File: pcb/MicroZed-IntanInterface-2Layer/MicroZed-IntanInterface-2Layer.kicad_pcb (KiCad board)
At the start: 2 copper layers, 100.3 x 135.4 mm, 107 parts, among them J1 Screw_Terminal_01x02, J2 Conn_02x05_Odd_Even, J4 USB_C_Receptacle_USB2.0_16P, J7 GND header for probes, Q1 BSS138, Q2 BSS138, Q3 BSS138, Q4 BSS138, SW1 SW_MEC_5E, SW2 SW_MEC_5E, U1 AP331A, U2 TLV62568DDC, U3 FT230XS, U9 TLV62568DDC

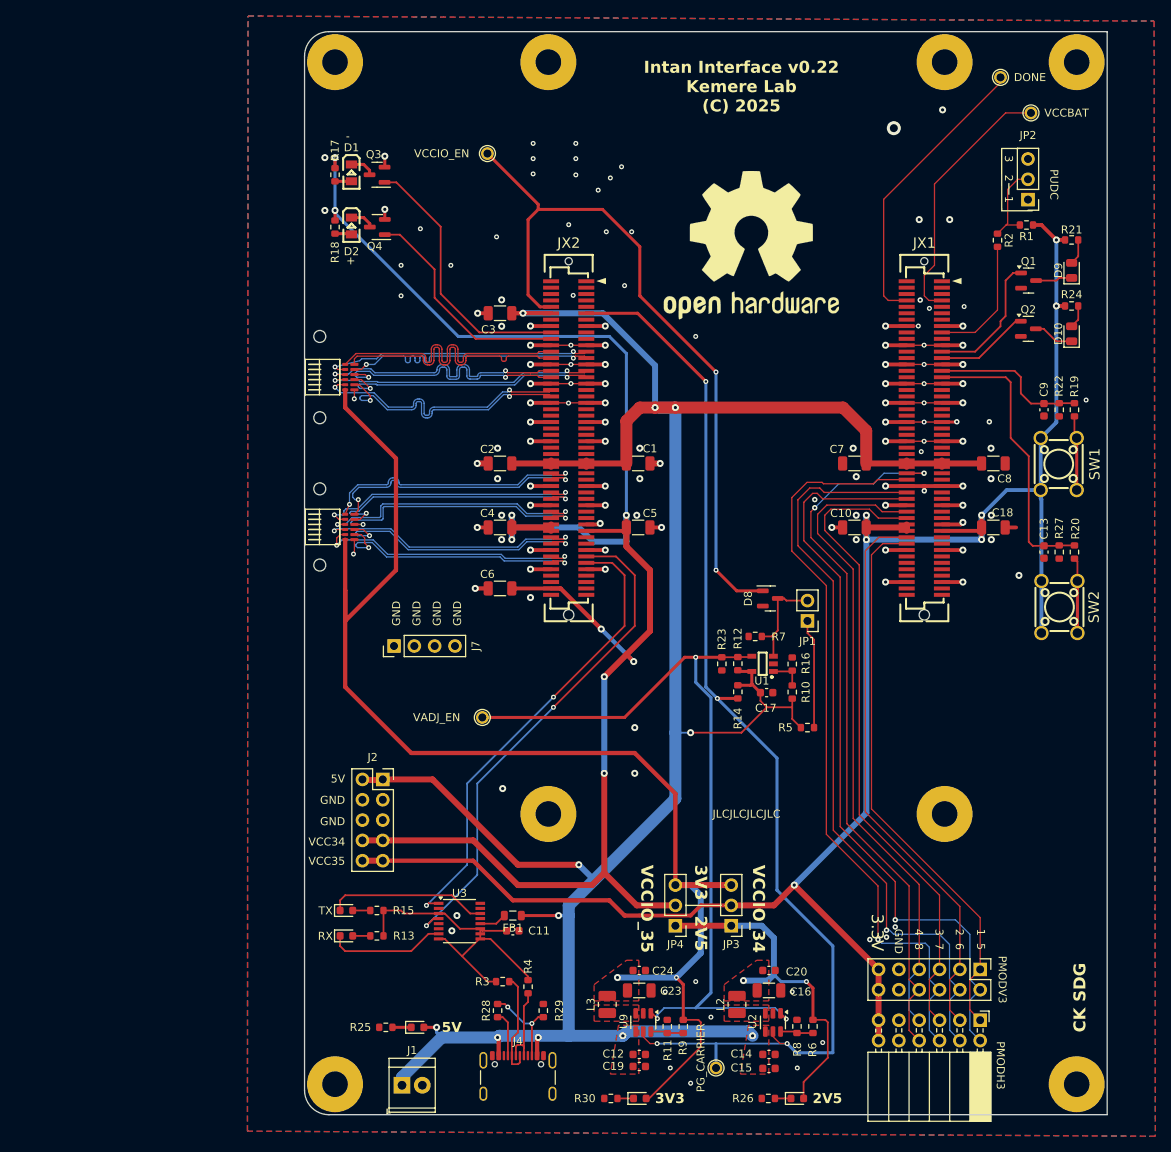
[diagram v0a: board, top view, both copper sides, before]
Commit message: Updated PCB after v0.22 bug fixes
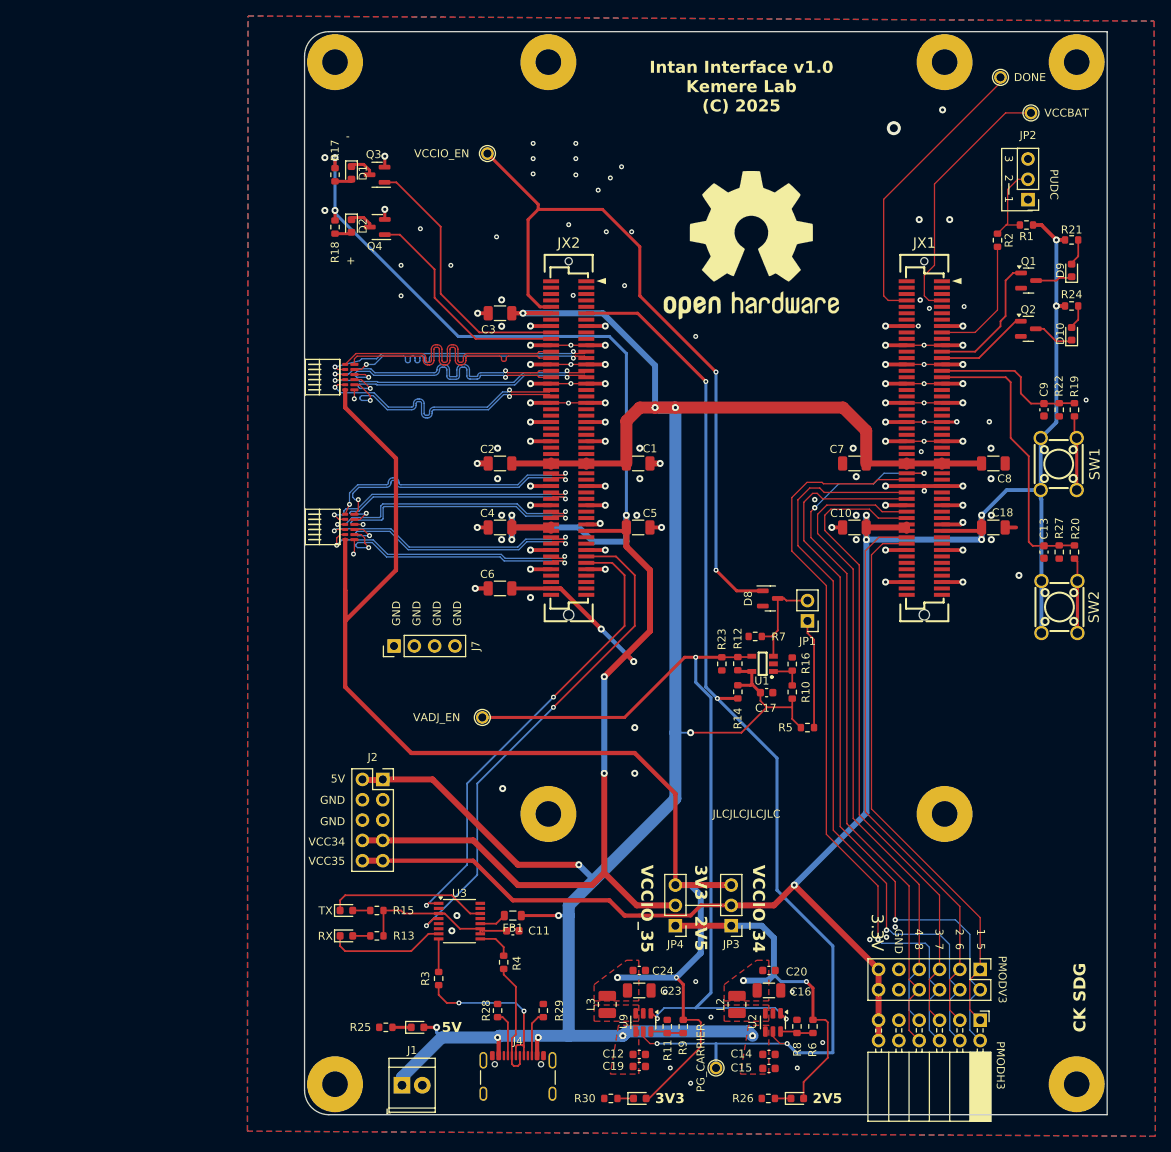
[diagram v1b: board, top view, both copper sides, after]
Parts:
- removed REF** (x4): MountingHole_2.1mm, MountingHole:MountingHole_2.1mm
- D1: value LED yellow -> LED0; footprint Viktor:LED0805 -> LED_SMD:LED_0603_1608Metric
- D10: value LED 4 -> LED3; footprint LED_SMD:LED_0805_2012Metric -> LED_SMD:LED_0603_1608Metric
- D2: value LED yellow -> LED1; footprint Viktor:LED0805 -> LED_SMD:LED_0603_1608Metric
- D9: value LED 3 -> LED2; footprint LED_SMD:LED_0805_2012Metric -> LED_SMD:LED_0603_1608Metric
- moved R3 8.01 mm to (52.3, 166.6), turned to 90 degrees
- moved R4 4.31 mm to (60.5, 164.6)
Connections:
- JX1 pad 23: /JX1_connections/LED3 -> /JX1_connections/LED2
- JX1 pad 25: /JX1_connections/LED4 -> /JX1_connections/LED3
- JX2 pad 18: /JX2_connections/LED1 -> /JX2_connections/LED0
- JX2 pad 20: /JX2_connections/LED2 -> /JX2_connections/LED1
- Q1 pad 1: /JX1_connections/LED3 -> /JX1_connections/LED2
- Q2 pad 1: /JX1_connections/LED4 -> /JX1_connections/LED3
- Q3 pad 1: /JX2_connections/LED1 -> /JX2_connections/LED0
- Q4 pad 1: /JX2_connections/LED2 -> /JX2_connections/LED1
- R28 pad 2: Net-(J4-CC2) -> GND
- R3 pad 1: USB_D- -> USB_D+
- R3 pad 2: Net-(U3-3V3OUT) -> Net-(U3-USBDP)
- R4 pad 1: USB_D+ -> USB_D-
- R4 pad 2: Net-(U3-3V3OUT) -> Net-(U3-USBDM)
- U3 pad 8: Net-(U3-3V3OUT) -> Net-(U3-USBDP)
- U3 pad 9: Net-(U3-3V3OUT) -> Net-(U3-USBDM)
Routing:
- net /JX2_connections/LED0: track 0.00 -> 33.5 mm
- net /JX2_connections/LED2: track 28.3 -> 0.00 mm
- net Net-(U3-3V3OUT): track 41.8 -> 20.3 mm
- net /JX1_connections/LED2: track 0.00 -> 16.9 mm
- net /JX1_connections/LED4: track 11.8 -> 0.00 mm
- net USB_D+: track 10.5 -> 20.6 mm, vias 0 -> 2
- net Net-(J4-CC2): track 11.1 -> 5.78 mm, vias 2 -> 0
- net /JX2_connections/LED1: track 33.5 -> 28.3 mm
- net /JX1_connections/LED3: track 16.9 -> 11.8 mm
- net Net-(U3-USBDM): track 0.00 -> 4.43 mm
- net Net-(U3-USBDP): track 0.00 -> 4.13 mm
- net USB_D-: track 13.3 -> 15.0 mm
- net VCCIO_35: track 221.2 -> 220.5 mm
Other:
- board text added: "Intan Interface v1.0 Kemere Lab (C) 2025"
- board text removed: "Intan Interface v0.22 Kemere Lab (C) 2025"

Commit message: Updates for version 1.0 to ship to UMich
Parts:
- removed JP1: Jumper_2_Open, Connector_PinHeader_2.54mm:PinHeader_1x02_P2.54mm_Vertical
- removed JP3, JP4: Jumper_3_Bridged12, Connector_PinHeader_2.54mm:PinHeader_1x03_P2.54mm_Vertical
- removed OpenHW logo: OSHW-Logo2_24.3x20mm_SilkScreen, Symbol:OSHW-Logo2_24.3x20mm_SilkScreen
- added JP5: SolderJumper_2_Open, Jumper:SolderJumper-2_P1.3mm_Open_RoundedPad1.0x1.5mm, B.Cu at (101.6, 86.6)
- added REF**: RICE_OWL_LOGO, ELEC327-Kicad:RICE_OWL_LOGO, F.Cu at (46.5, 78.0)
- added REF**: RICE_OWL_LOGO, ELEC327-Kicad:RICE_OWL_LOGO, F.Cu at (88.1, 114.0)
- added SW3: SW_SPDT, Button_Switch_SMD:SW_SPDT_PCM12, F.Cu at (101.6, 146.1)
- added SW4: SW_SPDT, Button_Switch_SMD:SW_SPDT_PCM12, F.Cu at (82.5, 146.1)
- C1, C16, C23: value 22uF 10V -> 22uF 25V
- C10, C18, C2, C3, C4, C5, C6, C7, C8: value 22uF -> 22uF 25V
- C11, C13, C15, C17, C19, C20, C24, C9: footprint Capacitor_SMD:C_0603_1608Metric -> Capacitor_SMD:C_0402_1005Metric
- H1, H2, H3, H4, H5, H6, H7, H8: footprint Viktor:MountingHole_3.2mm_Pad_7mm -> MountingHole:MountingHole_3.2mm_M3_Pad
- JP2: moved to B.Cu
- L2, L3: footprint Inductor_SMD:L_1008_2520Metric -> Inductor_SMD:L_1210_3225Metric
- R1, R5: value 1K -> 1k 1%; footprint Resistor_SMD:R_0603_1608Metric -> Resistor_SMD:R_0402_1005Metric
- R10: value 5K6 1% -> 5.6k 1%; footprint Resistor_SMD:R_0603_1608Metric -> Resistor_SMD:R_0402_1005Metric
- R11, R14, R6, R8, R9: footprint Resistor_SMD:R_0603_1608Metric -> Resistor_SMD:R_0402_1005Metric
- R12: value 3K -> 3k; footprint Resistor_SMD:R_0603_1608Metric -> Resistor_SMD:R_0402_1005Metric
- R13, R15: value 133R -> 150 1%; footprint Resistor_SMD:R_0603_1608Metric -> Resistor_SMD:R_0402_1005Metric
- R16: value 1K 1% -> 1k 1%; footprint Resistor_SMD:R_0603_1608Metric -> Resistor_SMD:R_0402_1005Metric
- R17, R18, R21, R24: value 150R -> 150 1%; footprint Resistor_SMD:R_0603_1608Metric -> Resistor_SMD:R_0402_1005Metric
- R19, R20: value 100R -> 150 1%; footprint Resistor_SMD:R_0603_1608Metric -> Resistor_SMD:R_0402_1005Metric
- R2: value 100R -> 100 1%; footprint Resistor_SMD:R_0603_1608Metric -> Resistor_SMD:R_0402_1005Metric
- R22, R27: value 3K3 -> 3k; footprint Resistor_SMD:R_0603_1608Metric -> Resistor_SMD:R_0402_1005Metric
- R23: value 100K -> 100k 1%; footprint Resistor_SMD:R_0603_1608Metric -> Resistor_SMD:R_0402_1005Metric
- R25: value 4K87 -> 1k 1%; footprint Resistor_SMD:R_0603_1608Metric -> Resistor_SMD:R_0402_1005Metric
- R26, R30: value 1K54 -> 1k 1%; footprint Resistor_SMD:R_0603_1608Metric -> Resistor_SMD:R_0402_1005Metric
- R28, R29: value 5K1 -> 5.1k; footprint Resistor_SMD:R_0603_1608Metric -> Resistor_SMD:R_0402_1005Metric
- R3, R4: value 27R -> 27; footprint Resistor_SMD:R_0603_1608Metric -> Resistor_SMD:R_0402_1005Metric
- R7: value 10K -> 10k; footprint Resistor_SMD:R_0603_1608Metric -> Resistor_SMD:R_0402_1005Metric
- TP10, TP11, TP12, TP7, TP8: footprint Viktor:TestPoint__Drill1.0mm -> TestPoint:TestPoint_THTPad_D2.0mm_Drill1.0mm; moved to B.Cu
- U2, U9: value TLV62568DDC -> TLV62568PDRLR; footprint Package_TO_SOT_SMD:SOT-23-6 -> Package_TO_SOT_SMD:SOT-563
- moved J1 149.0 mm to (125.5, 52.8), turned to 180 degrees
- moved R30 133.6 mm to (101.1, 50.8), turned to 0 degrees
- moved D5 132.3 mm to (97.5, 50.8), turned to 180 degrees
- moved D4 132.2 mm to (77.8, 50.8), turned to 180 degrees
- moved R26 131.4 mm to (81.4, 50.8), turned to 0 degrees
- moved J4 128.6 mm to (49.8, 51.9), turned to 180 degrees
- moved C19 124.5 mm to (97.5, 54.8), turned to 0 degrees
- moved C15 123.9 mm to (81.3, 54.6), turned to 0 degrees
- moved C12 121.5 mm to (97.5, 56.3), turned to 180 degrees
- moved C14 120.4 mm to (81.3, 56.3), turned to 180 degrees
- moved TP10 119.8 mm to (88.9, 58.0), turned to 90 degrees
- moved R29 115.8 mm to (42.5, 57.1), turned to 180 degrees
- moved R8 114.8 mm to (77.7, 59.4)
- moved R11 113.9 mm to (94.0, 59.4)
- moved U9 113.6 mm to (97.3, 60.2), turned to 90 degrees
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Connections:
- D1 pad 2: Net-(D1-A) -> VCCIO_35
- D2 pad 2: Net-(D2-A) -> VCCIO_35
- H1 pad 1: unconnected-(H1-Pad1) -> GND
- H2 pad 1: unconnected-(H2-Pad1) -> GND
- H3 pad 1: unconnected-(H3-Pad1) -> GND
- H4 pad 1: unconnected-(H4-Pad1) -> GND
- H5 pad 1: unconnected-(H5-Pad1) -> GND
- H6 pad 1: unconnected-(H6-Pad1) -> GND
- H7 pad 1: unconnected-(H7-Pad1) -> GND
- H8 pad 1: unconnected-(H8-Pad1) -> GND
- Q3 pad 3: Net-(D1-K) -> Net-(Q3-D)
- Q4 pad 3: Net-(D2-K) -> Net-(Q4-D)
- R17 pad 1: VCCIO_35 -> Net-(D1-K)
- R17 pad 2: Net-(D1-A) -> Net-(Q3-D)
- R18 pad 1: VCCIO_35 -> Net-(D2-K)
- R18 pad 2: Net-(D2-A) -> Net-(Q4-D)
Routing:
- net +2V5: track 44.0 -> 128.3 mm, vias 2 -> 4
- net PG_CARRIER: track 142.5 -> 76.5 mm, vias 4 -> 3
- net /VADJ_EN: track 101.9 -> 48.4 mm, vias 3 -> 2
- net +3V3: track 164.7 -> 215.8 mm, vias 2 -> 7
- net VCCIO_EN: track 90.2 -> 42.4 mm, vias 2 -> 1
- net Net-(JX1-DONE): track 36.5 -> 8.70 mm
- net /JX1_connections/SWITCH2: track 35.7 -> 9.99 mm
- net /JX2_connections/IO_L23P: track 63.5 -> 87.4 mm, vias 2 -> 0
- net /JX2_connections/IO_L23N: track 58.6 -> 82.4 mm, vias 2 -> 0
- net Net-(JX1-VCCBATT): track 32.7 -> 9.42 mm
- net VCCIO_34: track 231.1 -> 251.0 mm
- net USB_D+: track 20.6 -> 6.26 mm
- net Net-(SW1-A): track 9.32 -> 23.6 mm
- net /JX1_connections/IO_L24N: track 69.9 -> 83.4 mm, vias 0 -> 1
- net /JX1_connections/PUDC_B: track 16.0 -> 29.0 mm
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- added copper zone on In1.Cu, net GND
- added copper zone on In2.Cu, net GND
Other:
- board size 100.3 x 135.4 mm -> 100.3 x 101.6 mm
- copper layers 2 -> 4
- board text added: "+5V"
- board text added: "2V5 | 3V3"
- board text added: "HS1"
- board text added: "HS2"
- board text added: "Intan Interface Kemere Lab (C) 2026 Rev 1.0"
- board text added: "Short to test power without MicroZed"
- board text added: "VCCIO_34 (3V3) GND 8 4 7 3 6 2 5 1"
- board text removed: "-"
- board text removed: "3.3V"
- board text removed: "4"
- board text removed: "5"
- board text removed: "6"
- board text removed: "7"
- board text removed: "8"
- board text removed: "Intan Interface v1.0 Kemere Lab (C) 2025"
- board text removed: "JLCJLCJLCJLC"
